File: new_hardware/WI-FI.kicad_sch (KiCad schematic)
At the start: 1 part, among them U12 AP6212

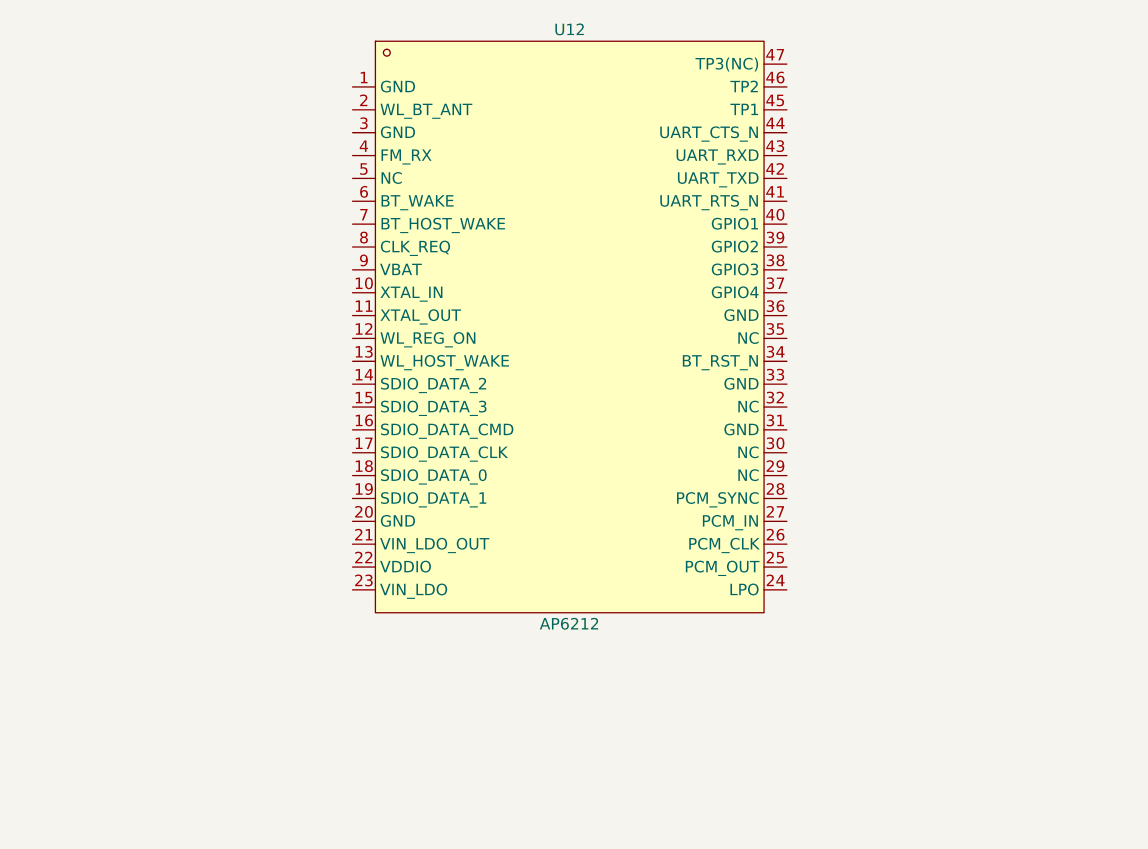
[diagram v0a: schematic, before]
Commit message: device tree is changed
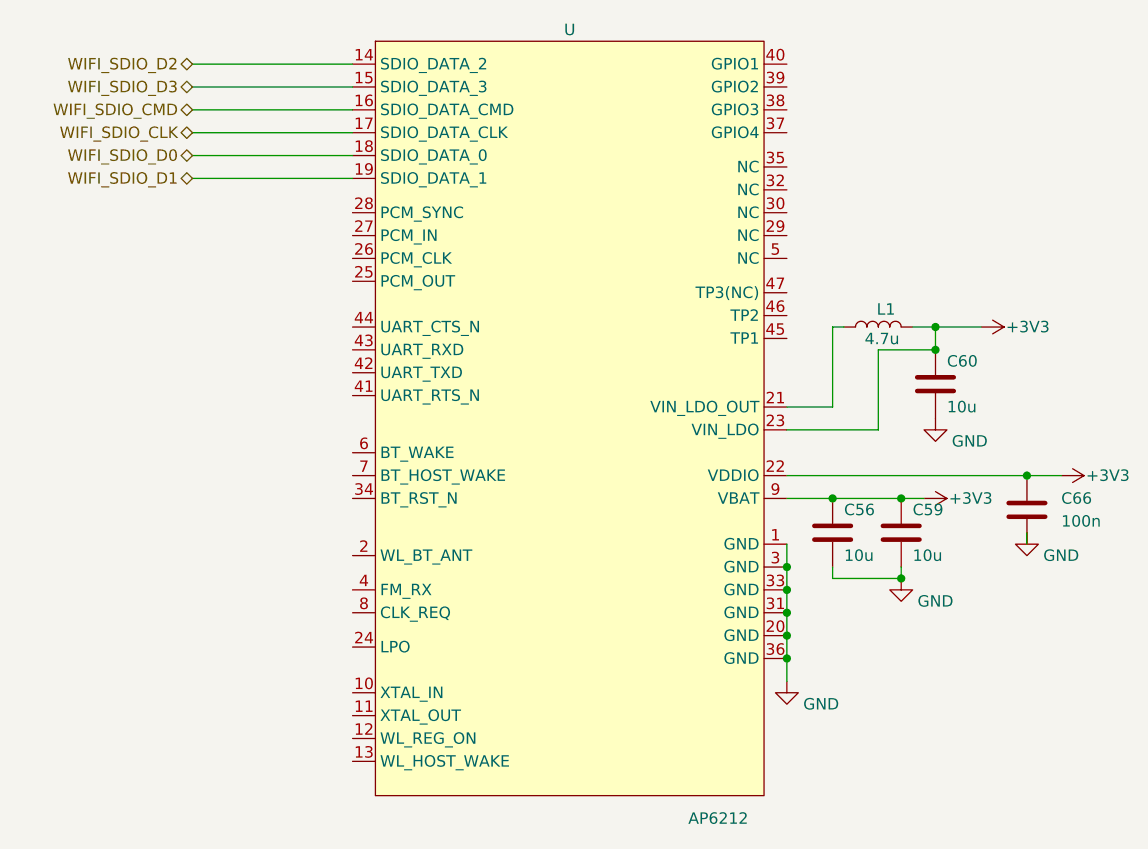
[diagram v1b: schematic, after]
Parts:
- added C56, C59, C60: 10u, rlib_passive:C_0603_1608Metric, symbol rlib_passive:C
- added C66: 100n, rlib_passive:C_0603_1608Metric, symbol rlib_passive:C
- added L1: 4.7u, rlib_passive:IND_LQH32PN4R7NN0L, symbol rlib_passive:L
- U: renamed from U12; JLC Part (none) -> Extended Part; LCSC Part (none) -> C2798300; Manufacturer AMPAK -> AMPAK(正基科技)
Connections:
- net GND: now reaches U.1 (GND)
- net GND: now also U.20 (GND), U.3 (GND), U.31 (GND), U.33 (GND), U.36 (GND), C56.2, C59.2, C60.2, C66.2
- net WIFI_SDIO_D2: now reaches U.14 (SDIO_DATA_2)
- net WIFI_SDIO_D3: now reaches U.15 (SDIO_DATA_3)
- net WIFI_SDIO_CMD: now reaches U.16 (SDIO_DATA_CMD)
- net WIFI_SDIO_CLK: now reaches U.17 (SDIO_DATA_CLK)
- net WIFI_SDIO_D0: now reaches U.18 (SDIO_DATA_0)
- net WIFI_SDIO_D1: now reaches U.19 (SDIO_DATA_1)
- net at U.21 (VIN_LDO_OUT): now also L1.1
- net +3V3: now reaches U.22 (VDDIO)
- net +3V3: now also U.23 (VIN_LDO), U.9 (VBAT), C56.1, C59.1, C60.1, C66.1, L1.2
